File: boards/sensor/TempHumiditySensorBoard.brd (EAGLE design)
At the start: 61 x 25.4 mm, 12 parts

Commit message: QR Code appears on schematic, has 'QR' identifier
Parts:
- removed U$7: (no value), QR-git.io-vRFkn:QR-HTTP://GIT.IO/VRFKN
- added QR1: QR-HTTP://GIT.IO/VRFKN, QR-git.io-vRFkn:QR-HTTP://GIT.IO/VRFKN
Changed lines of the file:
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@@
 <element name="U$5" library="fiducial" package="FID1MM" value="" x="55.88" y="22.86"/>
 <element name="U$6" library="JQI_Logo" package="JQI_LOGO_NEGATIVE-SILKSCREEN" value="" x="30.48" y="1.27" rot="MR90"/>
-<element name="U$7" library="QR-git.io-vRFkn" package="QR-HTTP://GIT.IO/VRFKN" value="" x="34.29" y="16.51" rot="MR0"/>
+<element name="QR1" library="QR-git.io-vRFkn" package="QR-HTTP://GIT.IO/VRFKN" value="QR-HTTP://GIT.IO/VRFKN" x="34.29" y="15.24" rot="MR0">
+<attribute name="QR_DEST" value="http://git.io/vRFkn" x="34.29" y="15.24" size="1.778" layer="28" rot="MR0" display="off"/>
+</element>
 </elements>
 <signals>

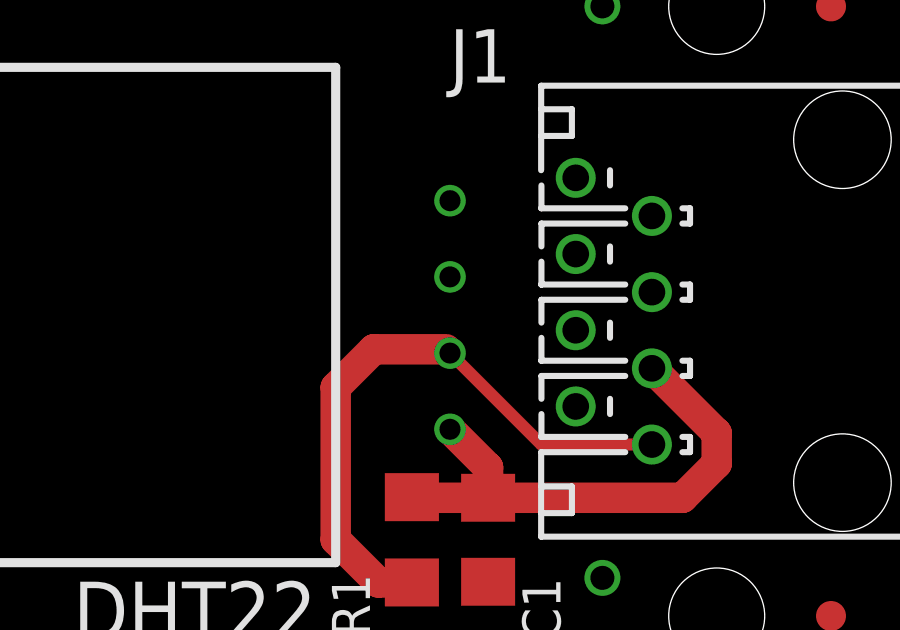
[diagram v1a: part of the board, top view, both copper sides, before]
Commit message: MacroFab files and BOM
Added BOMs for use with eagle-config and production files for MacroFab.

DSB
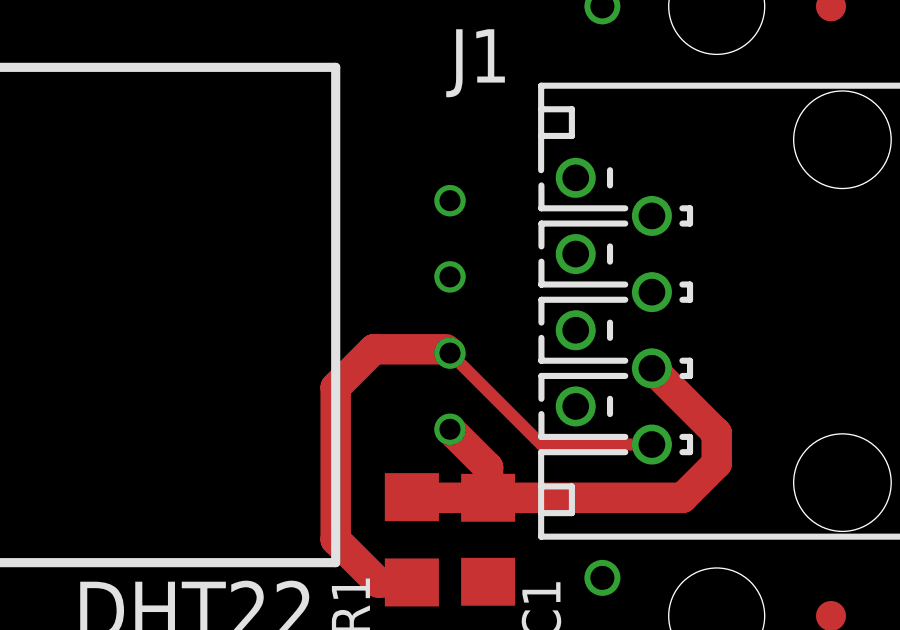
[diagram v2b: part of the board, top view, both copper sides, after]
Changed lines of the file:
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@@
 <?xml version="1.0" encoding="utf-8"?>
 <!DOCTYPE eagle SYSTEM "eagle.dtd">
-<eagle version="6.6.0">
+<eagle version="8.5.0">
 <drawing>
 <settings>
 <setting alwaysvectorfont="no"/>
+<setting keepoldvectorfont="yes"/>
 <setting verticaltext="up"/>
 </settings>
@@
 </class>
 </classes>
-<designrules name="oshpark">
-<description language="de">&lt;b&gt;EAGLE Design Rules&lt;/b&gt;
-&lt;p&gt;
-Die Standard-Design-Rules sind so gewählt, dass sie für
-die meisten Anwendungen passen. Sollte ihre Platine
-besondere Anforderungen haben, treffen Sie die erforderlichen
-Einstellungen hier und speichern die Design Rules unter
-einem neuen Namen ab.</description>
-<description language="en">&lt;b&gt;Laen's PCB Order Design Rules&lt;/b&gt;
-&lt;p&gt;
-Please make sure your boards conform to these design rules.</description>
+<designrules name="MF_Standard_2_Layer">
+<description language="en">&lt;b&gt;MacroFab, INC. EAGLE Design Rules&lt;/b&gt;
+&lt;p&gt;This DRC check is for 2-Layer Standard Capability boards to be manufactured through the MacroFab, INC. service.</description>
 <param name="layerSetup" value="(1*16)"/>
-<param name="mtCopper" value="0.0356mm 0.0356mm 0.0356mm 0.0356mm 0.0356mm 0.0356mm 0.0356mm 0.0356mm 0.0356mm 0.0356mm 0.0356mm 0.0356mm 0.0356mm 0.0356mm 0.0356mm 0.0356mm"/>
-<param name="mtIsolate" value="1.5011mm 0.1499mm 0.2007mm 0.1499mm 0.2007mm 0.1499mm 0.2007mm 0.1499mm 0.2007mm 0.1499mm 0.2007mm 0.1499mm 0.2007mm 0.1499mm 0.2007mm"/>
-<param name="mdWireWire" value="6mil"/>
-<param name="mdWirePad" value="6mil"/>
-<param name="mdWireVia" value="6mil"/>
-<param name="mdPadPad" value="6mil"/>
-<param name="mdPadVia" value="6mil"/>
-<param name="mdViaVia" value="6mil"/>
-<param name="mdSmdPad" value="6mil"/>
-<param name="mdSmdVia" value="6mil"/>
-<param name="mdSmdSmd" value="6mil"/>
+<param name="mtCopper" value="0.035mm 0.0175mm 0.035mm 0.035mm 0.035mm 0.035mm 0.035mm 0.035mm 0.035mm 0.035mm 0.035mm 0.035mm 0.035mm 0.035mm 0.0175mm 0.035mm"/>
+<param name="mtIsolate" value="1.5mm 1.1mm 0.2mm 0.15mm 0.2mm 0.15mm 0.2mm 0.15mm 0.2mm 0.15mm 0.2mm 0.15mm 0.2mm 0.15mm 0.2mm"/>
+<param name="mdWireWire" value="5mil"/>
+<param name="mdWirePad" value="5mil"/>
+<param name="mdWireVia" value="5mil"/>
+<param name="mdPadPad" value="5mil"/>
+<param name="mdPadVia" value="5mil"/>
+<param name="mdViaVia" value="5mil"/>
+<param name="mdSmdPad" value="0mil"/>
+<param name="mdSmdVia" value="0mil"/>
+<param name="mdSmdSmd" value="0mil"/>
 <param name="mdViaViaSameLayer" value="8mil"/>
 <param name="mnLayersViaInSmd" value="2"/>
-<param name="mdCopperDimension" value="15mil"/>
-<param name="mdDrill" value="6mil"/>
+<param name="mdCopperDimension" value="10mil"/>
+<param name="mdDrill" value="10mil"/>
 <param name="mdSmdStop" value="0mil"/>
-<param name="msWidth" value="6mil"/>
-<param name="msDrill" value="13mil"/>
-<param name="msMicroVia" value="13mil"/>
+<param name="msWidth" value="5mil"/>
+<param name="msDrill" value="12mil"/>
+<param name="msMicroVia" value="12mil"/>
 <param name="msBlindViaRatio" value="0.5"/>
 <param name="rvPadTop" value="0.25"/>
@@
 <param name="rvMicroViaOuter" value="0.25"/>
 <param name="rvMicroViaInner" value="0.25"/>
-<param name="rlMinPadTop" value="7mil"/>
+<param name="rlMinPadTop" value="6mil"/>
 <param name="rlMaxPadTop" value="20mil"/>
-<param name="rlMinPadInner" value="7mil"/>
+<param name="rlMinPadInner" value="6mil"/>
 <param name="rlMaxPadInner" value="20mil"/>
-<param name="rlMinPadBottom" value="7mil"/>
+<param name="rlMinPadBottom" value="6mil"/>
 <param name="rlMaxPadBottom" value="20mil"/>
-<param name="rlMinViaOuter" value="7mil"/>
+<param name="rlMinViaOuter" value="6mil"/>
 <param name="rlMaxViaOuter" value="20mil"/>
-<param name="rlMinViaInner" value="7mil"/>
+<param name="rlMinViaInner" value="6mil"/>
 <param name="rlMaxViaInner" value="20mil"/>
-<param name="rlMinMicroViaOuter" value="4mil"/>
+<param name="rlMinMicroViaOuter" value="6mil"/>
 <param name="rlMaxMicroViaOuter" value="20mil"/>
-<param name="rlMinMicroViaInner" value="4mil"/>
+<param name="rlMinMicroViaInner" value="6mil"/>
 <param name="rlMaxMicroViaInner" value="20mil"/>
 <param name="psTop" value="-1"/>
 <param name="psBottom" value="-1"/>
-<param name="psFirst" value="-1"/>
+<param name="psFirst" value="0"/>
 <param name="psElongationLong" value="100"/>
 <param name="psElongationOffset" value="100"/>
 <param name="mvStopFrame" value="1"/>
 <param name="mvCreamFrame" value="0"/>
-<param name="mlMinStopFrame" value="3mil"/>
-<param name="mlMaxStopFrame" value="3mil"/>
+<param name="mlMinStopFrame" value="2mil"/>
+<param name="mlMaxStopFrame" value="2mil"/>
 <param name="mlMinCreamFrame" value="0mil"/>
 <param name="mlMaxCreamFrame" value="0mil"/>
-<param name="mlViaStopLimit" value="0mil"/>
+<param name="mlViaStopLimit" value="25mil"/>
 <param name="srRoundness" value="0"/>
 <param name="srMinRoundness" value="0mil"/>
@@
 <param name="dpMaxLengthDifference" value="10mm"/>
 <param name="dpGapFactor" value="2.5"/>
-<param name="checkGrid" value="0"/>
 <param name="checkAngle" value="0"/>
 <param name="checkFont" value="1"/>
-<param name="checkRestrict" value="1"/>
+<param name="checkRestrict" value="0"/>
+<param name="checkStop" value="0"/>
+<param name="checkValues" value="0"/>
 <param name="useDiameter" value="13"/>
 <param name="maxErrors" value="50"/>
@@
 <pass name="Default">
 <param name="RoutingGrid" value="50mil"/>
+<param name="AutoGrid" value="1"/>
+<param name="Efforts" value="0"/>
+<param name="TopRouterVariant" value="1"/>
 <param name="tpViaShape" value="round"/>
 <param name="PrefDir.1" value="*"/>
@@
 </autorouter>
 <elements>
-<element name="DHT22" library="dht22" package="DHT22-H" value="DHT22-H" x="43.18" y="12.573" rot="R90"/>
+<element name="DHT22" library="dht22" package="DHT22-H" value="DHT22-H" x="43.18" y="12.573" rot="R90">
+<attribute name="PARTNO" value="385" x="43.18" y="12.573" size="1.778" layer="27" rot="R90" display="off"/>
+</element>
 <element name="J1" library="con-amp" package="555164-1" value="" x="55.118" y="12.7" smashed="yes" rot="R90">
 <attribute name="NAME" x="45.212" y="22.098" size="1.778" layer="25" rot="R180"/>
+<attribute name="PARTNO" value="555164-1" x="55.118" y="12.7" size="1.778" layer="27" rot="R90" display="off"/>
 <attribute name="VALUE" x="58.928" y="22.86" size="1.778" layer="27" rot="R180"/>
 </element>
 <element name="C1" library="resistor" package="C1206" value="100nF" x="44.45" y="5.08" smashed="yes" rot="R270">
 <attribute name="NAME" x="45.593" y="3.81" size="1.27" layer="25" rot="R270"/>
+<attribute name="PARTNO" value="CL31B104JBCNNNC" x="44.45" y="5.08" size="1.778" layer="27" rot="R270" display="off"/>
 <attribute name="VALUE" x="42.037" y="6.35" size="1.27" layer="27" rot="R270"/>
 </element>
 <element name="R1" library="resistor" package="R1206" value="1k" x="41.91" y="5.08" smashed="yes" rot="R90">
 <attribute name="NAME" x="39.243" y="3.937" size="1.27" layer="25" rot="R270"/>
+<attribute name="PARTNO" value="ERJ-8ENF2001V" x="41.91" y="5.08" size="1.778" layer="27" rot="R90" display="off"/>
 <attribute name="VALUE" x="44.323" y="3.683" size="1.27" layer="27" rot="R90"/>
 </element>
@@
 </element>
 <element name="H1" library="JQI-holes" package="MOUNT-HOLE-1/4&quot;-FREE" value="MOUNT-HOLE-1/4&quot;-FREE" x="6.35" y="12.7">
+<attribute name="HOLE-FIT" value="Free" x="6.35" y="12.7" size="1.778" layer="27" display="off"/>
 <attribute name="HOLE-SIZE" value="1/4&quot;" x="6.35" y="12.7" size="1.778" layer="27" display="off"/>
 <attribute name="HOLE-WASHER" value="" x="6.35" y="12.7" size="1.778" layer="27" display="off"/>
-<attribute name="HOLE-FIT" value="Free" x="6.35" y="12.7" size="1.778" layer="27" display="off"/>
 </element>
 <element name="U$1" library="fiducial" package="FID1MM" value="" x="6.35" y="2.54"/>
